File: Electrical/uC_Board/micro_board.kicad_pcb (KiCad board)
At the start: 2 copper layers, 45 x 18 mm, 0 parts

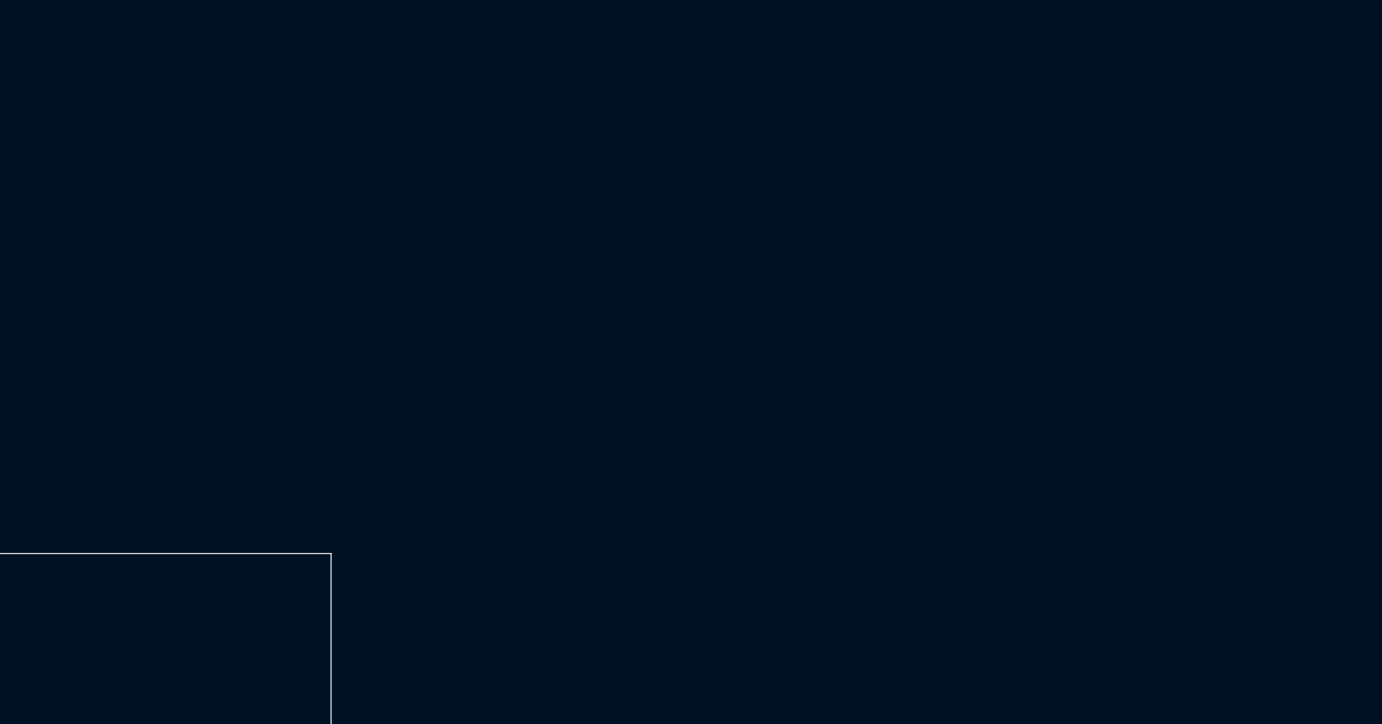
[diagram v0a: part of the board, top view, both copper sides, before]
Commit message: added atmega footprint, started PCB
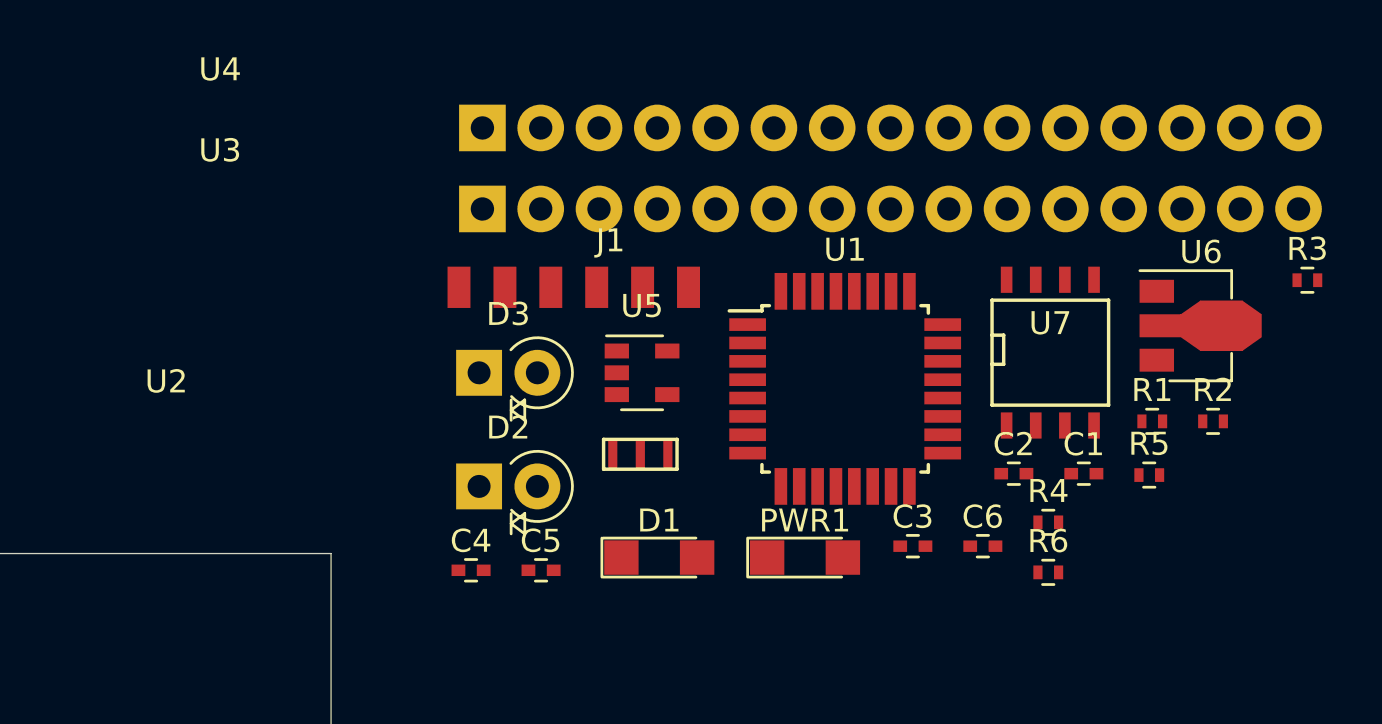
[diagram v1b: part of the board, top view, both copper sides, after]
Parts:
- added C1: 100nF, Capacitors_SMD:C_0402, F.Cu at (177.8, 96.5)
- added C2: 1uF, Capacitors_SMD:C_0402, F.Cu at (174.8, 96.5)
- added C3: 4.7uF, Capacitors_SMD:C_0402, F.Cu at (170.3, 99.7)
- added C4: 1uF, Capacitors_SMD:C_0402, F.Cu at (151.1, 100.7)
- added C5: 10uF, Capacitors_SMD:C_0402, F.Cu at (154.2, 100.7)
- added C6: 10uF, Capacitors_SMD:C_0402, F.Cu at (173.4, 99.7)
- added D1: YELLOW, LEDs:LED_1206, F.Cu at (159.3, 100.2)
- added D2: LED, Diodes_THT:D_T-1_P2.54mm_Vertical_KathodeUp, F.Cu at (151.4, 97.1)
- added D3: D_Photo, Diodes_THT:D_T-1_P2.54mm_Vertical_KathodeUp, F.Cu at (151.4, 92.1)
- added J1: card_edge_6p, hodgkin:card_edge_6p_single_side, F.Cu at (150.6, 88.4)
- added PWR1: GREEN, LEDs:LED_1206, F.Cu at (165.7, 100.2)
- added R1: 1k, Resistors_SMD:R_0402, F.Cu at (180.8, 94.2)
- added R2: 1k, Resistors_SMD:R_0402, F.Cu at (183.4, 94.2)
- added R3: 1k, Resistors_SMD:R_0402, F.Cu at (187.5, 88.1)
- added R4: 1k, Resistors_SMD:R_0402, F.Cu at (176.2, 98.6)
- added R5: R, Resistors_SMD:R_0402, F.Cu at (180.7, 96.6)
- added R6: 1M, Resistors_SMD:R_0402, F.Cu at (176.2, 100.8)
- added U1: ATmega328PB-AU, hodgkin:TQFP-32_7x7mm_P0.8mm, F.Cu at (167.4, 92.8)
- added U2: CSTNE16M0V530000R0, hodgkin:CSTNE16M0V530000R0, F.Cu at (156.9, 96.3)
- added U3: ArdStripNano, hodgkin:ArdNanoStrip, F.Cu at (150.3, 86.3)
- added U4: ArdStripNano, hodgkin:ArdNanoStrip, F.Cu at (150.3, 82.7)
- added U5: RN5RF33BA-TR-FE, TO_SOT_Packages_SMD:SOT-23-5, F.Cu at (158.6, 92.1)
- added U6: 2DA1213O-13, TO_SOT_Packages_SMD:SOT-89-3, F.Cu at (182.5, 90.1)
- added U7: AD8620-hodgkin, SMD_Packages:SOIC-8-N, F.Cu at (176.3, 91.2)

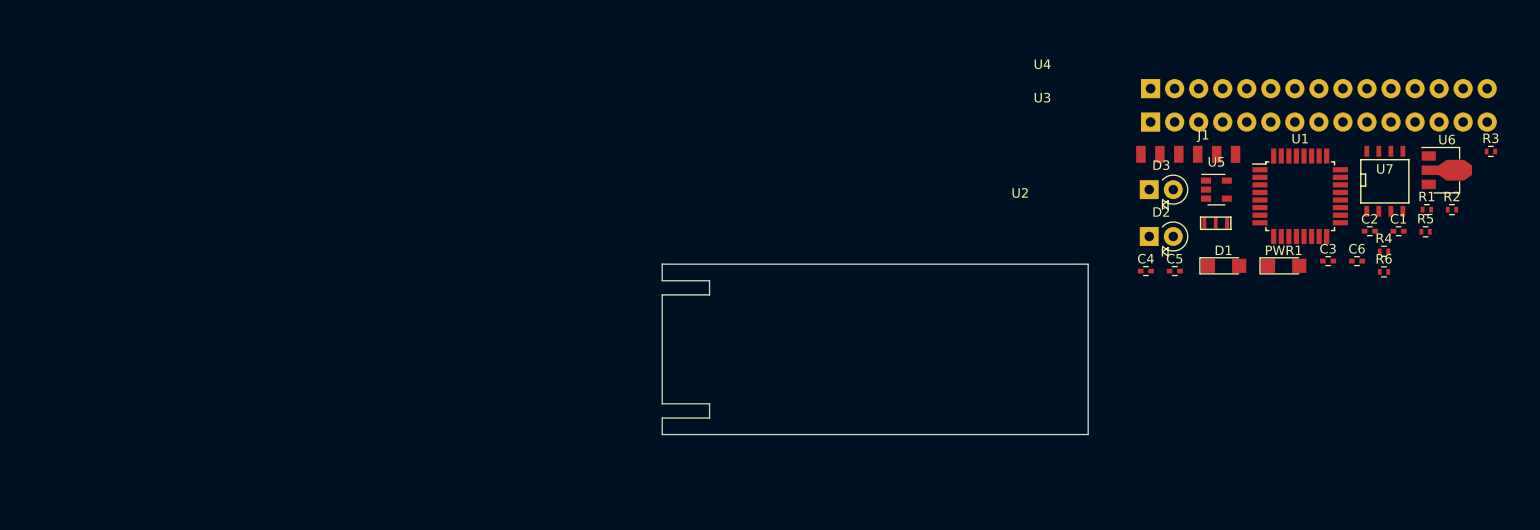
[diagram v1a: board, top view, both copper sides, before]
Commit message: started pcb layout
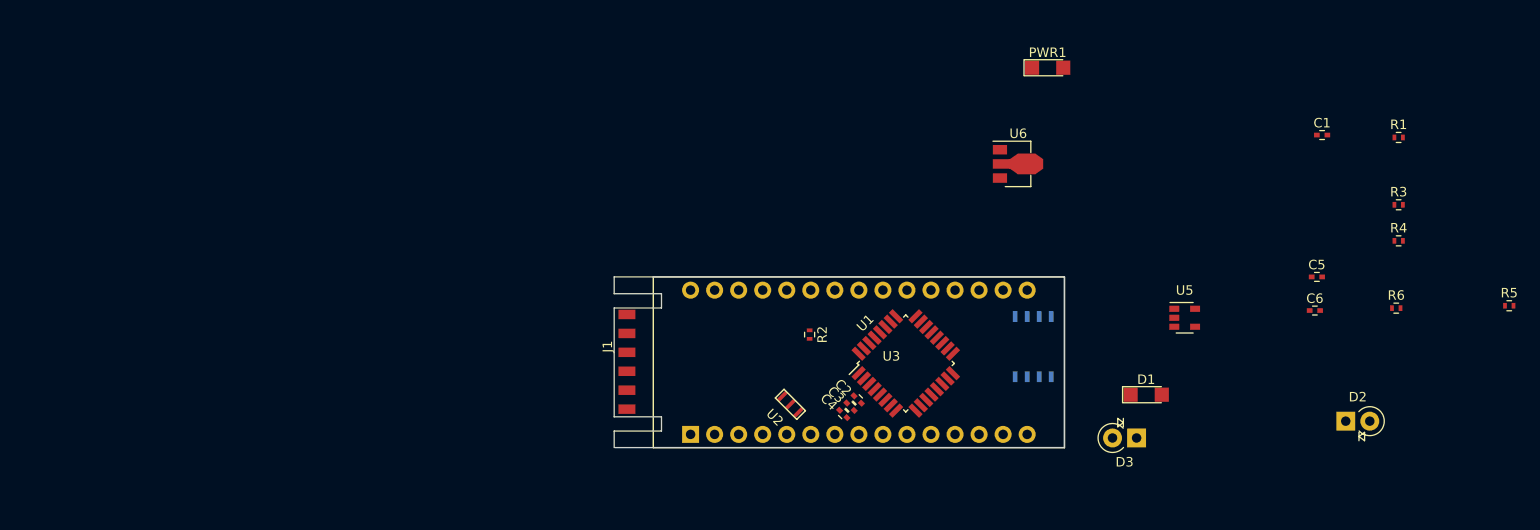
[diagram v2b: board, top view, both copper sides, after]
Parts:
- removed U4: ArdStripNano, hodgkin:ArdNanoStrip
- U7: moved to B.Cu
- moved R2 69.1 mm to (115.6, 107.4), turned to 270 degrees
- moved J1 60.6 mm to (96.3, 115.3), turned to 90 degrees
- moved C2 56.9 mm to (120.7, 114.3), turned to 135 degrees
- moved C3 52.8 mm to (119.9, 115.1), turned to 135 degrees
- moved U2 45.9 mm to (115.1, 115.5), turned to 135 degrees
- moved U6 45.3 mm to (137.2, 89.4)
- moved U1 45.3 mm to (125.7, 110.5), turned to 45 degrees
- moved U7 41.0 mm to (139.2, 108.7)
- moved C4 35.4 mm to (119.1, 115.8), turned to 135 degrees
- moved PWR1 32.6 mm to (140.7, 79.2)
- moved D2 28.5 mm to (172.2, 116.6)
- moved D3 26.3 mm to (150.1, 118.4), turned to 180 degrees
- moved U3 17.0 mm to (142.5, 101.3), turned to 180 degrees
- moved D1 15.9 mm to (151.1, 113.8)
- moved C5 15.0 mm to (169.2, 101.3)
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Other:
- board size 45 x 18 mm -> 47.6 x 18 mm

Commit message: forgot to save before pushing
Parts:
- U7: moved to F.Cu
- moved R4 68.1 mm to (110.2, 105.7), turned to 90 degrees
- moved R1 67.2 mm to (114.3, 108.7)
- moved U5 49.8 mm to (105.4, 106.4)
- moved C1 47.5 mm to (126.5, 106.2), turned to 135 degrees
- moved R2 41.2 mm to (156.7, 106.9)
- moved U6 39.2 mm to (105.2, 112.0), turned to 90 degrees
- moved PWR1 37.7 mm to (113.8, 105.7), turned to 180 degrees
- moved U7 27.2 mm to (163.3, 121.2)
- moved C4 9.67 mm to (114.3, 124.2)
- moved C3 9.55 mm to (115.3, 123.4)
- moved C2 9.43 mm to (116.3, 122.7)
- moved U2 8.39 mm to (110.3, 122.3)
- moved U1 3.57 mm to (122.2, 110.4)
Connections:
- U3 pad 17: Net-(U3-Pad17) -> +3V3
- U3 pad 27: +5V -> +3V3
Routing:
- net /D12: track 0.00 -> 14.1 mm
- net /D11: track 0.00 -> 11.9 mm
- net /D10: track 0.00 -> 9.70 mm
- net /D9: track 0.00 -> 7.49 mm
- net /D8: track 0.00 -> 5.73 mm
- net /D7: track 0.00 -> 4.35 mm
- net /D6: track 0.00 -> 3.86 mm
- net /D5: track 0.00 -> 3.58 mm

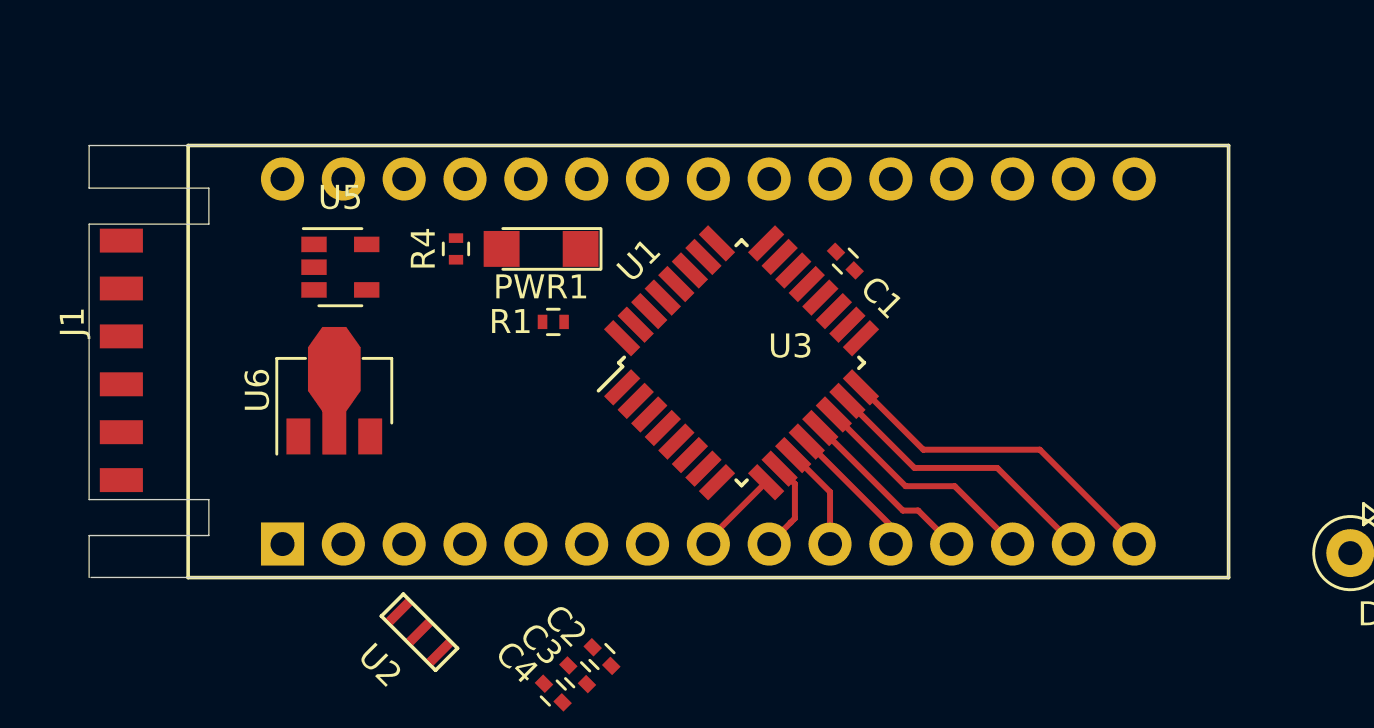
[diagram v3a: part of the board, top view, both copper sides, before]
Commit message: Minor arduino nano footprint modifications.
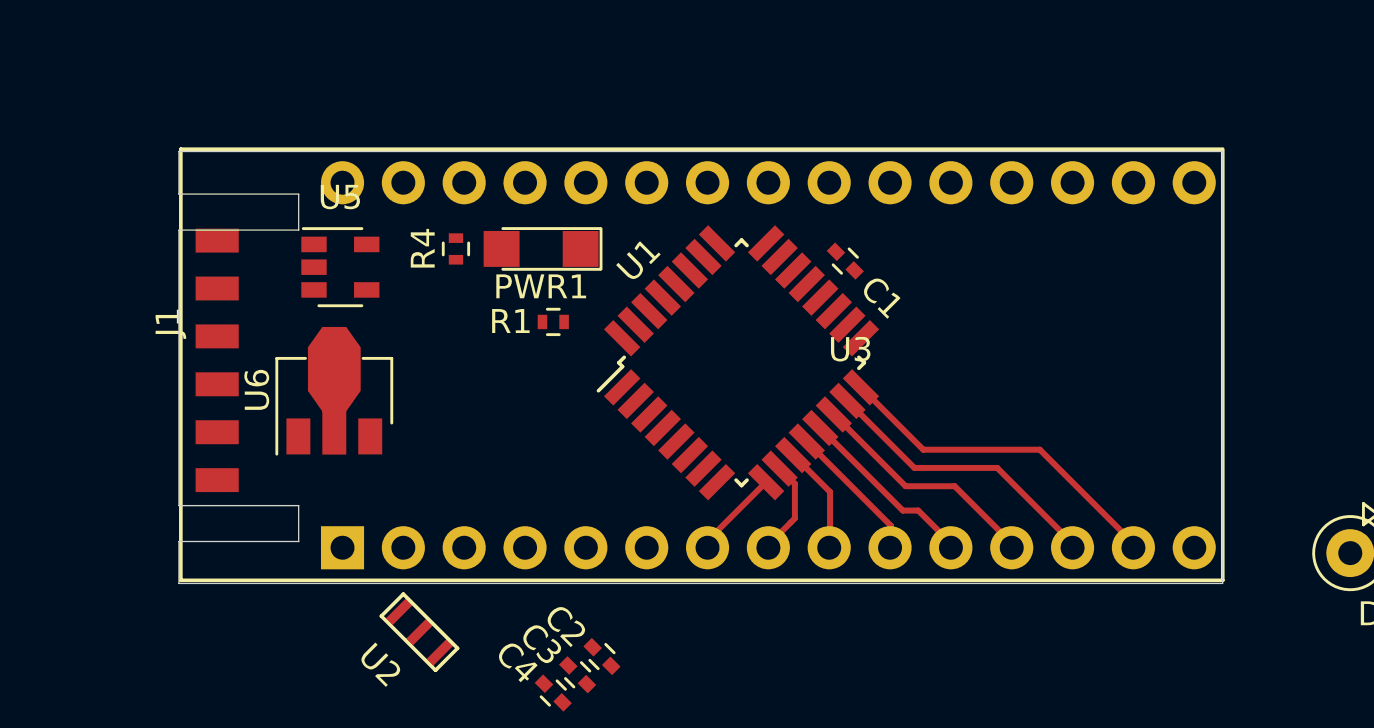
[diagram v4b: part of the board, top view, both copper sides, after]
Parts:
- moved J1 4.00 mm to (100.3, 115.3)
- moved U3 2.51 mm to (145.0, 101.5)
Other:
- board size 47.6 x 18 mm -> 43.6 x 18 mm

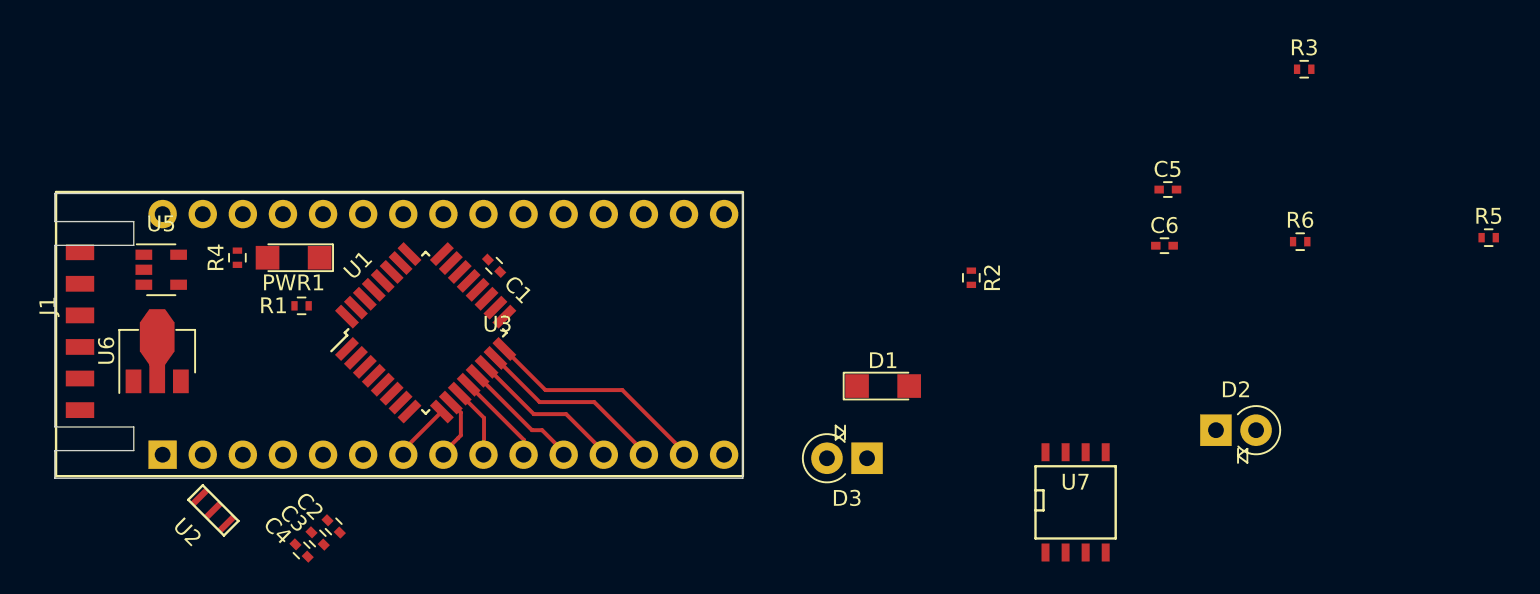
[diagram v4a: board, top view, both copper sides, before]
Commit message: changed 3.3v regulator to 5v regulator, laid things out on pcb
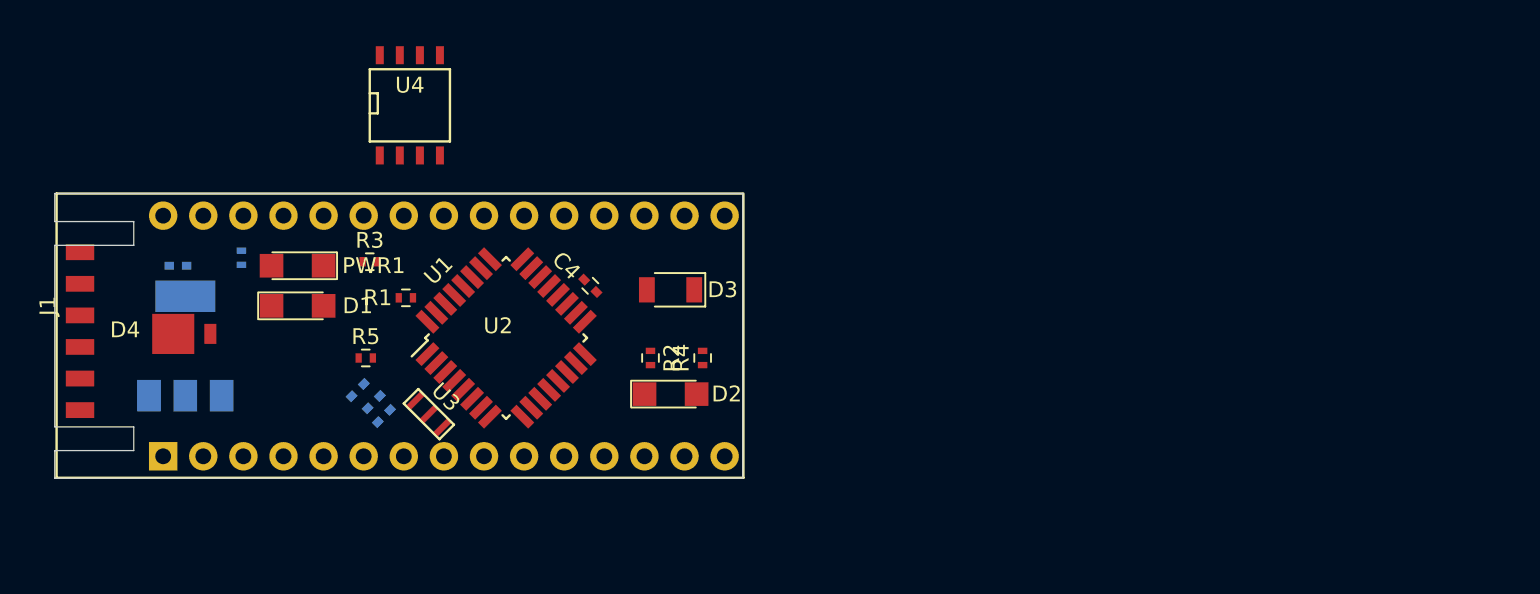
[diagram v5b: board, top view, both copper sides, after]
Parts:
- removed C6: 10uF, Capacitors_SMD:C_0402
- removed U6: 2DA1213O-13, TO_SOT_Packages_SMD:SOT-89-3
- removed U7: AD8620-hodgkin, SMD_Packages:SOIC-8-N
- added D4: D, hodgkin:DO-220AA-2, F.Cu at (106.2, 110.5)
- added U4: AD8620-hodgkin, SMD_Packages:SOIC-8-N, F.Cu at (121.2, 96.0)
- C1: value 100nF -> 1uF; moved to B.Cu
- C2: value 1uF -> 4.7uF; moved to B.Cu
- C3: value 4.7uF -> 1uF; moved to B.Cu
- C4: value 1uF -> 100nF
- C5: value 10uF -> 1uF; moved to B.Cu
- D2: footprint Diodes_THT:D_T-1_P2.54mm_Vertical_KathodeUp -> LEDs:LED_1206
- D3: footprint Diodes_THT:D_T-1_P2.54mm_Vertical_KathodeUp -> Diodes_SMD:D_1206
- R4: value 1k -> R
- R5: value R -> 1M
- R6: value 1M -> 1k; moved to B.Cu
- U2: value CSTNE16M0V530000R0 -> ArdStripNano; footprint hodgkin:CSTNE16M0V530000R0 -> hodgkin:ArdNanoStrip
- U3: value ArdStripNano -> CSTNE16M0V530000R0; footprint hodgkin:ArdNanoStrip -> hodgkin:CSTNE16M0V530000R0
- U5: value RN5RF33BA-TR-FE -> LM1117MPX-5.0; footprint TO_SOT_Packages_SMD:SOT-23-5 -> TO_SOT_Packages_SMD:SOT-223; moved to B.Cu
- moved R5 71.5 mm to (118.4, 112.0)
- moved R6 67.1 mm to (110.5, 105.7), turned to 90 degrees
- moved C5 62.9 mm to (106.5, 106.2)
- moved R3 60.4 mm to (118.6, 105.9)
- moved U2 40.5 mm to (145.0, 101.6), turned to 180 degrees
- moved D1 37.4 mm to (114.0, 108.7)
- moved D2 34.6 mm to (137.7, 114.3)
- moved R4 30.1 mm to (139.7, 112.0)
- moved U3 25.7 mm to (124.0, 116.2), turned to 135 degrees
- moved C4 24.8 mm to (132.6, 107.4)
- moved R2 20.9 mm to (136.4, 112.0)
- moved D3 16.4 mm to (137.7, 107.7)
- moved C1 11.8 mm to (119.5, 115.7), turned to 225 degrees
- moved C3 9.74 mm to (117.9, 114.0), turned to 225 degrees
- moved C2 8.27 mm to (118.9, 114.8), turned to 225 degrees
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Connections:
- C1 pad 1: Net-(C1-Pad1) -> +5V
- C2 pad 1: +3V3 -> +5V
- C3 pad 1: +3V3 -> +5V
- C4 pad 1: +3V3 -> Net-(C4-Pad1)
- C5 pad 1: VCC -> +5V
- J1 pad 1: /D12 -> VCC
- J1 pad 2: +5V -> /D13
- J1 pad 3: /D13 -> /D12
- R4 pad 1: Net-(PWR1-Pad2) -> Net-(D2-Pad2)
- R4 pad 2: +3V3 -> /TX
- R5 pad 1: Net-(D2-Pad2) -> Net-(D3-Pad1)
- R5 pad 2: /TX -> /RX
- R6 pad 1: Net-(D3-Pad1) -> Net-(PWR1-Pad2)
- R6 pad 2: /RX -> +5V
- U1 pad 18: +3V3 -> +5V
- U1 pad 20: Net-(C1-Pad1) -> Net-(C4-Pad1)
- U1 pad 4: +3V3 -> +5V
- U1 pad 6: +3V3 -> +5V
- U2 pad 1: Net-(U1-Pad8) -> /D1
- U2 pad 2: Net-(U1-Pad7) -> /D0
- U2 pad 3: GND -> /RESET
- U3 pad 1: /D1 -> Net-(U1-Pad8)
- U3 pad 2: /D0 -> Net-(U1-Pad7)
- U3 pad 3: /RESET -> GND
- U5 pad 1: GND -> Net-(U5-Pad1)
- U5 pad 2: VCC -> +5V
- U5 pad 3: +3V3 -> VCC
- U5 pad 4: Net-(U5-Pad4) -> +5V
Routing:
- net /D12: track 14.1 -> 0.00 mm
- net /D11: track 11.9 -> 0.00 mm
- net /D10: track 9.70 -> 0.00 mm
- net /D9: track 7.49 -> 0.00 mm
- net /D8: track 5.73 -> 0.00 mm
- net /D7: track 4.35 -> 0.00 mm
- net /D6: track 3.86 -> 0.00 mm
- net /D5: track 3.58 -> 0.00 mm
